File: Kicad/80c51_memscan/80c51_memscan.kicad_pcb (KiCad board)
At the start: 2 copper layers, 0 parts

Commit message: Fixes and changes to needed to get the PCB going (change J1 symbol to match footprints. Mounting holes added to schematic to match PCB requirements, etc.
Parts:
- added C1: 10uF, Capacitor_SMD:C_0603_1608Metric_Pad1.05x0.95mm_HandSolder, F.Cu at (47.8, 66.2)
- added C2: .1uF, Capacitor_SMD:C_0603_1608Metric_Pad1.05x0.95mm_HandSolder, F.Cu at (84.8, 43.8)
- added D1: LED, LED_SMD:LED_0603_1608Metric, F.Cu at (45.0, 61.5)
- added J1: Conn_02x16_Male, Connector_PinHeader_2.54mm:PinHeader_2x16_P2.54mm_Vertical, F.Cu at (92.4, 46.0)
- added J2: Conn_01x02_Male, Connector_PinHeader_2.54mm:PinHeader_1x02_P2.54mm_Vertical, F.Cu at (43.5, 67.2)
- added MK1: MountingHole, MountingHole:MountingHole_8.4mm_M8, F.Cu at (31.8, 31.8)
- added MK10: MountingHole, MountingHole:MountingHole_8.4mm_M8, F.Cu at (57.1, 108.0)
- added MK11: MountingHole, MountingHole:MountingHole_8.4mm_M8, F.Cu at (82.5, 108.0)
- added MK12: MountingHole, MountingHole:MountingHole_8.4mm_M8, F.Cu at (108.0, 108.0)
- added MK2: MountingHole, MountingHole:MountingHole_8.4mm_M8, F.Cu at (57.1, 31.8)
- added MK3: MountingHole, MountingHole:MountingHole_8.4mm_M8, F.Cu at (82.5, 31.8)
- added MK4: MountingHole, MountingHole:MountingHole_8.4mm_M8, F.Cu at (108.0, 31.8)
- added MK5: MountingHole, MountingHole:MountingHole_8.4mm_M8, F.Cu at (31.8, 57.1)
- added MK6: MountingHole, MountingHole:MountingHole_8.4mm_M8, F.Cu at (108.0, 57.1)
- added MK7: MountingHole, MountingHole:MountingHole_8.4mm_M8, F.Cu at (31.8, 82.5)
- added MK8: MountingHole, MountingHole:MountingHole_8.4mm_M8, F.Cu at (108.0, 82.5)
- added MK9: MountingHole, MountingHole:MountingHole_8.4mm_M8, F.Cu at (31.8, 108.0)
- added R1: 8.2k, Capacitor_SMD:C_0603_1608Metric_Pad1.05x0.95mm_HandSolder, F.Cu at (90.3, 93.3)
- added R10: R, Capacitor_SMD:C_0603_1608Metric_Pad1.05x0.95mm_HandSolder, F.Cu at (42.5, 61.6)
- added R2: 2.2k, Capacitor_SMD:C_0603_1608Metric_Pad1.05x0.95mm_HandSolder, F.Cu at (190.3, 51.4)
- added R3: 2.2k, Capacitor_SMD:C_0603_1608Metric_Pad1.05x0.95mm_HandSolder, F.Cu at (186.9, 51.4)
- added R4: 2.2k, Capacitor_SMD:C_0603_1608Metric_Pad1.05x0.95mm_HandSolder, F.Cu at (183.6, 51.4)
- added R5: 2.2k, Capacitor_SMD:C_0603_1608Metric_Pad1.05x0.95mm_HandSolder, F.Cu at (95.9, 39.2)
- added R6: 2.2k, Capacitor_SMD:C_0603_1608Metric_Pad1.05x0.95mm_HandSolder, F.Cu at (102.0, 45.0)
- added R7: 2.2k, Capacitor_SMD:C_0603_1608Metric_Pad1.05x0.95mm_HandSolder, F.Cu at (100.8, 41.3)
- added R8: 2.2k, Capacitor_SMD:C_0603_1608Metric_Pad1.05x0.95mm_HandSolder, F.Cu at (86.3, 64.2)
- added R9: 2.2k, Capacitor_SMD:C_0603_1608Metric_Pad1.05x0.95mm_HandSolder, F.Cu at (100.1, 73.3)
- added SW1: SW_SPST, Button_Switch_THT:SW_DIP_SPSTx01_Slide_9.78x4.72mm_W7.62mm_P2.54mm, F.Cu at (43.7, 48.9)
- added U1: P80C51FA-4N,112, P80C51FA-4N_112:DIP254P1524X470-40, F.Cu at (77.5, 94.7)
- added Y1: 4-12Mhz, Crystal:Crystal_SMD_0603-2Pin_6.0x3.5mm_HandSoldering, F.Cu at (44.1, 92.2)
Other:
- board outline added: 88.9 x 88.9 mm
- net class Default: clearance 0.2 -> 0.1524; trace_width 0.25 -> 0.3048; via_dia 0.8 -> 0.6858; via_drill 0.4 -> 0.3302
- rule pad_to_mask_clearance: 0.051 -> 0
- rule trace_clearance: 0.2 -> 0.1524
- rule trace_min: 0.2 -> 0.1524
- rule via_min_drill: 0.3 -> 0.254
- rule via_min_size: 0.4 -> 0.508

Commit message: Initial PCB layout complete.
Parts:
- D1: footprint LED_SMD:LED_0603_1608Metric -> LED_SMD:LED_0603_1608Metric_Pad1.05x0.95mm_HandSolder
- J2: footprint Connector_PinHeader_2.54mm:PinHeader_1x02_P2.54mm_Vertical -> Connector_Molex:Molex_KK-254_AE-6410-02A_1x02_P2.54mm_Vertical
- moved R2 103.0 mm to (87.4, 47.6), turned to 180 degrees
- moved R3 99.5 mm to (87.4, 50.8), turned to 180 degrees
- moved R4 96.2 mm to (87.4, 54.0), turned to 180 degrees
- moved R1 48.6 mm to (48.0, 69.2), turned to 180 degrees
- moved R7 26.0 mm to (87.4, 63.5), turned to 180 degrees
- moved R6 21.2 mm to (87.4, 60.3), turned to 180 degrees
- moved R5 19.9 mm to (87.4, 57.1), turned to 180 degrees
- moved R9 13.2 mm to (87.4, 69.8), turned to 180 degrees
- moved R10 10.5 mm to (43.8, 72.0)
- moved J2 10.1 mm to (46.4, 76.8), turned to 270 degrees
- moved SW1 5.47 mm to (45.7, 54.0)
- moved C2 2.85 mm to (87.4, 42.5)
- moved R8 2.70 mm to (87.4, 66.7), turned to 180 degrees
- moved Y1 2.35 mm to (45.7, 90.5)
- moved J1 0.55 mm to (91.9, 45.7)
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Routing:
- net Earth: track 0.00 -> 172.8 mm
- net +5V: track 0.00 -> 76.7 mm
- net A8: track 0.00 -> 43.6 mm
- net A9: track 0.00 -> 38.2 mm
- net Net-(C1-Pad2): track 0.00 -> 30.9 mm
- net A10: track 0.00 -> 28.7 mm
- net A7: track 0.00 -> 26.0 mm
- net A6: track 0.00 -> 25.7 mm
- net A2: track 0.00 -> 25.5 mm
- net A5: track 0.00 -> 25.5 mm
- net A0: track 0.00 -> 25.3 mm
- net A4: track 0.00 -> 25.2 mm
- net A1: track 0.00 -> 25.1 mm
- net A3: track 0.00 -> 24.9 mm
- net A11: track 0.00 -> 20.8 mm
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- added copper zone on F.Cu, net Earth

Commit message: Changed the switch to be push button.
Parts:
- SW1: footprint Button_Switch_THT:SW_DIP_SPSTx01_Slide_9.78x4.72mm_W7.62mm_P2.54mm -> Button_Switch_SMD:SW_SPST_B3S-1000
- moved SW1 7.01 mm to (45.1, 47.0), turned to 270 degrees
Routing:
- net Net-(C1-Pad2): track 30.9 -> 41.2 mm
- net +5V: track 76.7 -> 85.1 mm

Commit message: Adding text.
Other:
- board text added: "80C51 Memory Scanner v1.0 (this way up)"
- board text added: "yusufm@"
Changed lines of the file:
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@@
   (general
     (thickness 1.6)
-    (drawings 6)
+    (drawings 11)
     (tracks 150)
     (zones 0)
@@
     (tags "mounting hole 8.4mm no annular m8")
     (attr virtual)
-    (fp_text reference MK10 (at 0 -9.4) (layer F.SilkS)
+    (fp_text reference MK10 (at 0 -9.4) (layer F.SilkS) hide
       (effects (font (size 1 1) (thickness 0.15)))
     )
@@
     (tags "mounting hole 8.4mm no annular m8")
     (attr virtual)
-    (fp_text reference MK9 (at 0 -9.4) (layer F.SilkS)
+    (fp_text reference MK9 (at 0 -9.4) (layer F.SilkS) hide
       (effects (font (size 1 1) (thickness 0.15)))
     )
@@
     (tags "mounting hole 8.4mm no annular m8")
     (attr virtual)
-    (fp_text reference MK8 (at 0 -9.4) (layer F.SilkS)
+    (fp_text reference MK8 (at 0 -9.4) (layer F.SilkS) hide
       (effects (font (size 1 1) (thickness 0.15)))
     )
@@
     (tags "mounting hole 8.4mm no annular m8")
     (attr virtual)
-    (fp_text reference MK7 (at 0 -9.4) (layer F.SilkS)
+    (fp_text reference MK7 (at 0 -9.4) (layer F.SilkS) hide
       (effects (font (size 1 1) (thickness 0.15)))
     )
@@
     (tags "mounting hole 8.4mm no annular m8")
     (attr virtual)
-    (fp_text reference MK6 (at 0 -9.4) (layer F.SilkS)
+    (fp_text reference MK6 (at 0 -9.4) (layer F.SilkS) hide
       (effects (font (size 1 1) (thickness 0.15)))
     )
@@
     (tags "mounting hole 8.4mm no annular m8")
     (attr virtual)
-    (fp_text reference MK5 (at 0 -9.4) (layer F.SilkS)
+    (fp_text reference MK5 (at 0 -9.4) (layer F.SilkS) hide
       (effects (font (size 1 1) (thickness 0.15)))
     )
@@
     (tags "mounting hole 8.4mm no annular m8")
     (attr virtual)
-    (fp_text reference MK4 (at 0 -9.4) (layer F.SilkS)
+    (fp_text reference MK4 (at 0 -9.4) (layer F.SilkS) hide
       (effects (font (size 1 1) (thickness 0.15)))
     )
@@
     (tags "mounting hole 8.4mm no annular m8")
     (attr virtual)
-    (fp_text reference MK3 (at 0 -9.4) (layer F.SilkS)
+    (fp_text reference MK3 (at 0 -9.4) (layer F.SilkS) hide
       (effects (font (size 1 1) (thickness 0.15)))
     )
@@
     (tags "mounting hole 8.4mm no annular m8")
     (attr virtual)
-    (fp_text reference MK2 (at 0 -9.4) (layer F.SilkS)
+    (fp_text reference MK2 (at 0 -9.4) (layer F.SilkS) hide
       (effects (font (size 1 1) (thickness 0.15)))
     )
@@
     (tags "mounting hole 8.4mm no annular m8")
     (attr virtual)
-    (fp_text reference MK1 (at 0 -9.4) (layer F.SilkS)
+    (fp_text reference MK1 (at 0 -9.4) (layer F.SilkS) hide
       (effects (font (size 1 1) (thickness 0.15)))
     )
@@
     (tags "mounting hole 8.4mm no annular m8")
     (attr virtual)
-    (fp_text reference MK11 (at 0 -9.4) (layer F.SilkS)
+    (fp_text reference MK11 (at 0 -9.4) (layer F.SilkS) hide
       (effects (font (size 1 1) (thickness 0.15)))
     )
@@
     (tags "mounting hole 8.4mm no annular m8")
     (attr virtual)
-    (fp_text reference MK12 (at 0 -9.4) (layer F.SilkS)
+    (fp_text reference MK12 (at 0 -9.4) (layer F.SilkS) hide
       (effects (font (size 1 1) (thickness 0.15)))
     )
@@
       (net 41 +5V))
   )
+  (gr_text yusufm@ (at 44.45 111.76) (layer F.SilkS)
+    (effects (font (size 1.5 1.5) (thickness 0.3)))
+  )
+  (gr_circle (center 59.69 43.815) (end 59.69 44.45) (layer F.SilkS) (width 0.2))
+  (gr_text "80C51 Memory Scanner\nv1.0 (this way up)" (at 84.455 93.98) (layer F.SilkS)
+    (effects (font (size 1.5 1.5) (thickness 0.3)) (justify left))
+  )
+  (gr_line (start 40.64 75.565) (end 41.91 75.565) (layer F.SilkS) (width 0.2))
+  (gr_line (start 41.275 74.93) (end 41.275 76.2) (layer F.SilkS) (width 0.2))
   (gr_line (start 45.085 66.675) (end 46.355 66.675) (layer F.SilkS) (width 0.2))
   (gr_line (start 45.72 66.04) (end 45.72 67.31) (layer F.SilkS) (width 0.2))

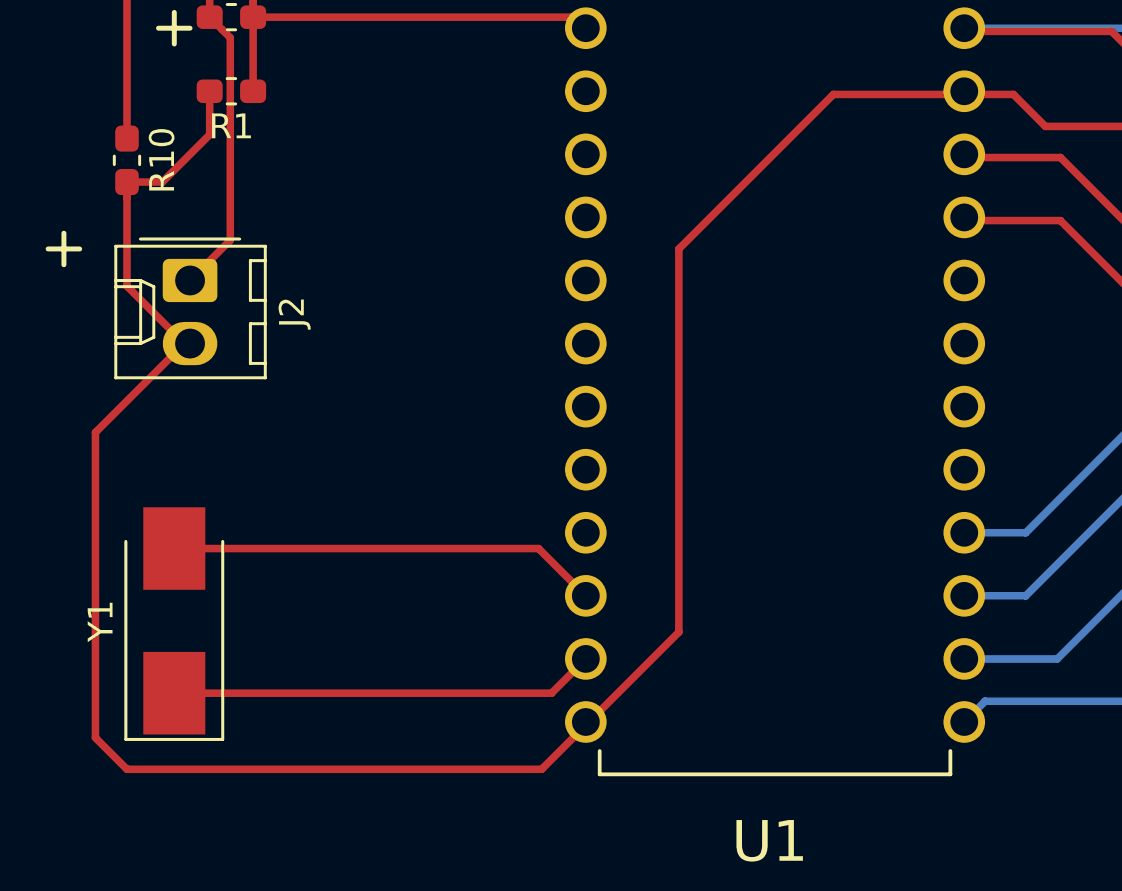
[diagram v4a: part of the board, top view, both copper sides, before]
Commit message: Added caps to xtal.
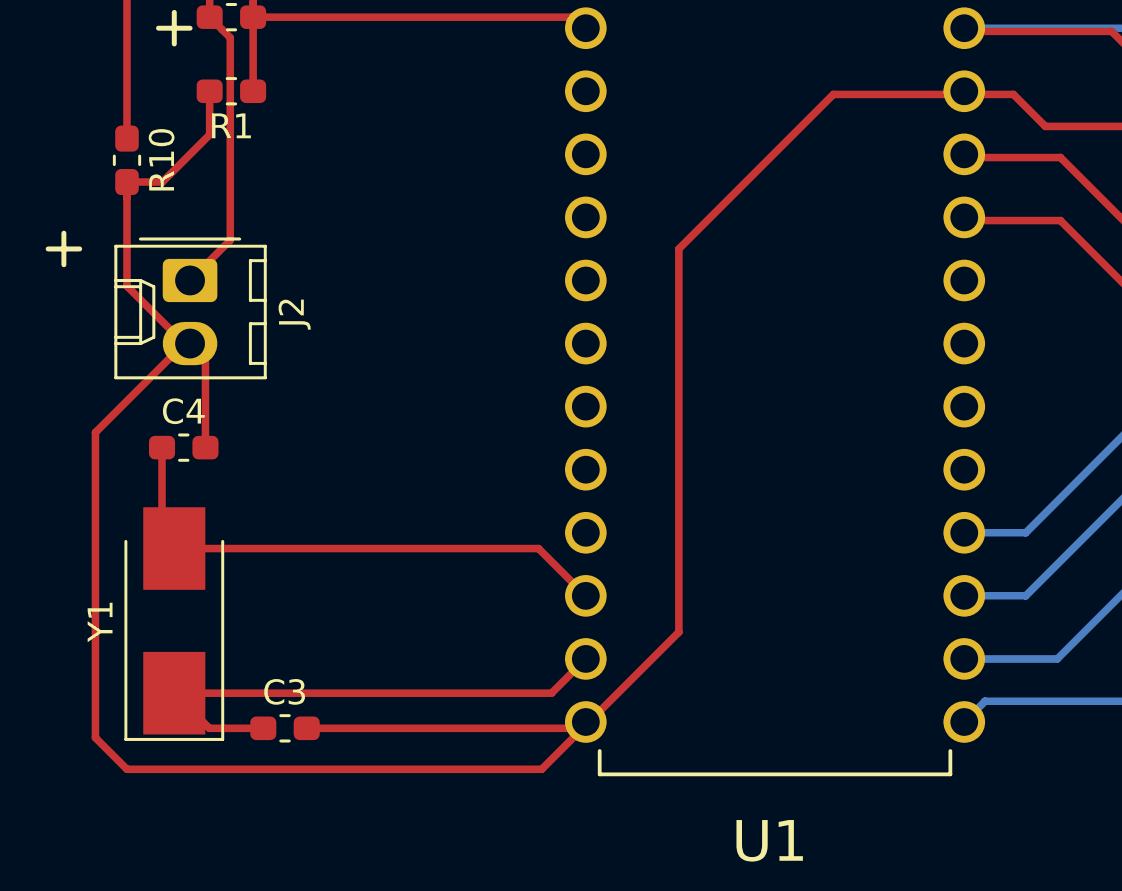
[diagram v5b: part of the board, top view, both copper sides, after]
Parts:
- added C3: 27pF, Capacitor_SMD:C_0603_1608Metric_Pad1.05x0.95mm_HandSolder, F.Cu at (50.2, 94.9)
- added C4: 27pF, Capacitor_SMD:C_0603_1608Metric_Pad1.05x0.95mm_HandSolder, F.Cu at (46.1, 83.6)
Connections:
- J1 pad 29: Net-(J1-Pad29) -> (no net)
- J1 pad 31: Net-(J1-Pad31) -> (no net)
- U1 pad 1: Net-(U1-Pad1) -> (no net)
- U1 pad 10: Net-(U1-Pad10) -> (no net)
- U1 pad 11: Net-(U1-Pad11) -> (no net)
- U1 pad 12: Net-(U1-Pad12) -> (no net)
- U1 pad 13: Net-(U1-Pad13) -> (no net)
- U1 pad 14: Net-(U1-Pad14) -> (no net)
- U1 pad 15: Net-(U1-Pad15) -> (no net)
- U1 pad 16: Net-(U1-Pad16) -> (no net)
- U1 pad 17: Net-(U1-Pad17) -> (no net)
- U1 pad 2: Net-(U1-Pad2) -> (no net)
- U1 pad 25: Net-(U1-Pad25) -> (no net)
- U1 pad 26: Net-(U1-Pad26) -> (no net)
- U1 pad 27: Net-(U1-Pad27) -> (no net)
- U1 pad 28: Net-(U1-Pad28) -> (no net)
- U1 pad 3: Net-(U1-Pad3) -> (no net)
- U1 pad 4: Net-(U1-Pad4) -> (no net)
- U1 pad 5: Net-(U1-Pad5) -> (no net)
- U1 pad 6: Net-(U1-Pad6) -> (no net)
- U1 pad 7: Net-(U1-Pad7) -> (no net)
- U1 pad 8: Net-(U1-Pad8) -> (no net)
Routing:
- net Earth: track 172.8 -> 188.6 mm
- net XTAL2: track 17.4 -> 21.6 mm
- net XTAL1: track 17.1 -> 21.3 mm
- net ALEn: vias 1 -> 0

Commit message: Fix minor typo.
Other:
- board text added: "80C51 Memory Scanner v1.0 (this side up)"
- board text removed: "80C51 Memory Scanner v1.0 (this way up)"
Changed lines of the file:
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@@
   )
   (gr_circle (center 59.69 43.815) (end 59.69 44.45) (layer F.SilkS) (width 0.2))
-  (gr_text "80C51 Memory Scanner\nv1.0 (this way up)" (at 84.455 93.98) (layer F.SilkS)
+  (gr_text "80C51 Memory Scanner\nv1.0 (this side up)" (at 84.455 93.98) (layer F.SilkS)
     (effects (font (size 1.5 1.5) (thickness 0.3)) (justify left))
   )
